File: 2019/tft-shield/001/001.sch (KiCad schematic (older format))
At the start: 7 parts, among them J1 CONN_01X08, Q1 S8050, U1 TFT_0.9680*160

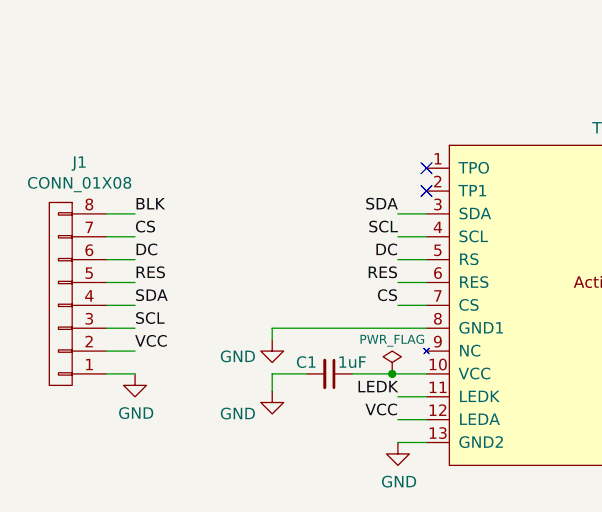
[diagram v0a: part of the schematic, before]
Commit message: Add Draw settings in Docs TFT
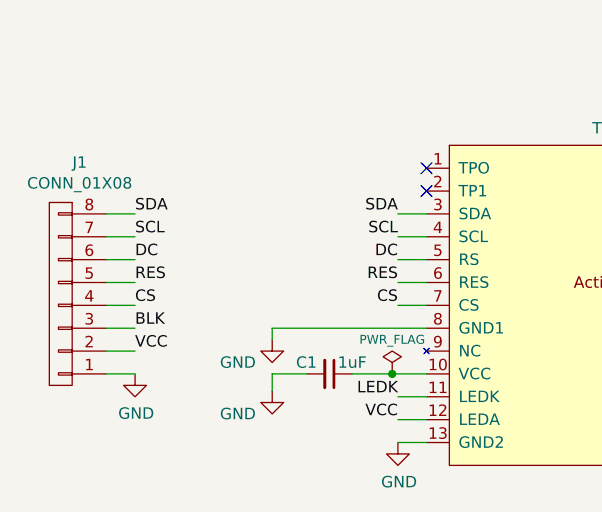
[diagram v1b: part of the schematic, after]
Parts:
- Q1: footprint Package_SO:SOIC-8_5.23x5.23mm_P1.27mm -> Package_TO_SOT_SMD:SOT-23
- U1: footprint (none) -> tft-shield:TFT_0.96_SPI
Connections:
- net BLK: now also J1.3 (P3); no longer J1.8 (P8)
- net CS: now also J1.4 (P4); no longer J1.7 (P7)
- net SCL: now also J1.7 (P7); no longer J1.3 (P3)
- net SDA: now also J1.8 (P8); no longer J1.4 (P4)
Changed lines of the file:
@@
 EESchema Schematic File Version 4
+LIBS:001-cache
 EELAYER 29 0
 EELAYER END
@@
 F 0 "U1" H 5825 4650 50  0000 L CNN
 F 1 "TFT_0.9680*160" H 5550 4525 50  0000 L CNN
-F 2 "" H 5875 3750 50  0001 C CNN
+F 2 "tft-shield:TFT_0.96_SPI" H 5875 3750 50  0001 C CNN
 F 3 "" H 5875 3750 50  0001 C CNN
 	1    5875 3750
@@
 F 0 "Q1" H 8340 3721 50  0000 L CNN
 F 1 "S8050" H 8340 3630 50  0000 L CNN
-F 2 "Package_SO:SOIC-8_5.23x5.23mm_P1.27mm" H 8350 3600 50  0001 L CIN
+F 2 "Package_TO_SOT_SMD:SOT-23" H 8350 3600 50  0001 L CIN
 F 3 "http://www.unisonic.com.tw/datasheet/S8050.pdf" H 8150 3675 50  0001 L CNN
 	1    8150 3675
@@
 Wire Wire Line
 	4150 3850 4825 3850
-$Comp
-L power:GND #PWR02
-U 1 1 5CE90EB8
-P 4150 3900
-F 0 "#PWR02" H 4150 3650 50  0001 C CNN
-F 1 "GND" H 4000 3825 50  0000 C CNN
-F 2 "" H 4150 3900 50  0001 C CNN
-F 3 "" H 4150 3900 50  0001 C CNN
-	1    4150 3900
-	1    0    0    -1
-$EndComp
 Wire Wire Line
 	4150 3850 4150 3900
@@
 Text Label 3550 3950 0    50   ~ 0
 VCC
-Text Label 3550 3850 0    50   ~ 0
+Text Label 3550 3450 0    50   ~ 0
 SCL
-Text Label 3550 3750 0    50   ~ 0
+Text Label 3550 3350 0    50   ~ 0
 SDA
 Text Label 3550 3650 0    50   ~ 0
@@
 Text Label 3550 3550 0    50   ~ 0
 DC
-Text Label 3550 3450 0    50   ~ 0
+Text Label 3550 3750 0    50   ~ 0
 CS
-Text Label 3550 3350 0    50   ~ 0
+Text Label 3550 3850 0    50   ~ 0
 BLK
 $Comp
@@
 Wire Wire Line
 	4675 4050 4825 4050
+$Comp
+L power:GND #PWR0101
+U 1 1 5CEF97E8
+P 4150 3900
+F 0 "#PWR0101" H 4150 3650 50  0001 C CNN
+F 1 "GND" H 4000 3800 50  0000 C CNN
+F 2 "" H 4150 3900 50  0001 C CNN
+F 3 "" H 4150 3900 50  0001 C CNN
+	1    4150 3900
+	1    0    0    -1
+$EndComp
 $EndSCHEMATC

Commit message: Add changes tft_shield
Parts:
- C1: symbol device:C_Small -> 001-rescue:C_Small-device
- J1: symbol conn:CONN_01X08 -> 001-rescue:CONN_01X08-conn
- Q1: symbol transistors:S8050 -> 001-rescue:S8050-transistors
- R1, R2, R3: symbol device:R_Small -> 001-rescue:R_Small-device
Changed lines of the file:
@@
 $EndComp
 $Comp
-L conn:CONN_01X08 J1
+L 001-rescue:CONN_01X08-conn J1
 U 1 1 5CE71D48
 P 3225 3700
@@
 	3425 4050 3550 4050
 $Comp
-L transistors:S8050 Q1
+L 001-rescue:S8050-transistors Q1
 U 1 1 5CE7D6CD
 P 8150 3675
@@
 $EndComp
 $Comp
-L device:R_Small R1
+L 001-rescue:R_Small-device R1
 U 1 1 5CE7DDEC
 P 7600 3675
@@
 $EndComp
 $Comp
-L device:R_Small R3
+L 001-rescue:R_Small-device R3
 U 1 1 5CE7E014
 P 8475 3350
@@
 Connection ~ 7825 3675
 $Comp
-L device:R_Small R2
+L 001-rescue:R_Small-device R2
 U 1 1 5CE7FBA5
 P 7825 3900
@@
 VCC
 $Comp
-L device:C_Small C1
+L 001-rescue:C_Small-device C1
 U 1 1 5CE8903B
 P 4400 4050
